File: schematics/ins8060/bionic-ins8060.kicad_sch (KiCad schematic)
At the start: 5 parts, among them J1 Bionic-P135, J2 Bionic-P245, U1 INS8060, U3 11AA010-I/TO

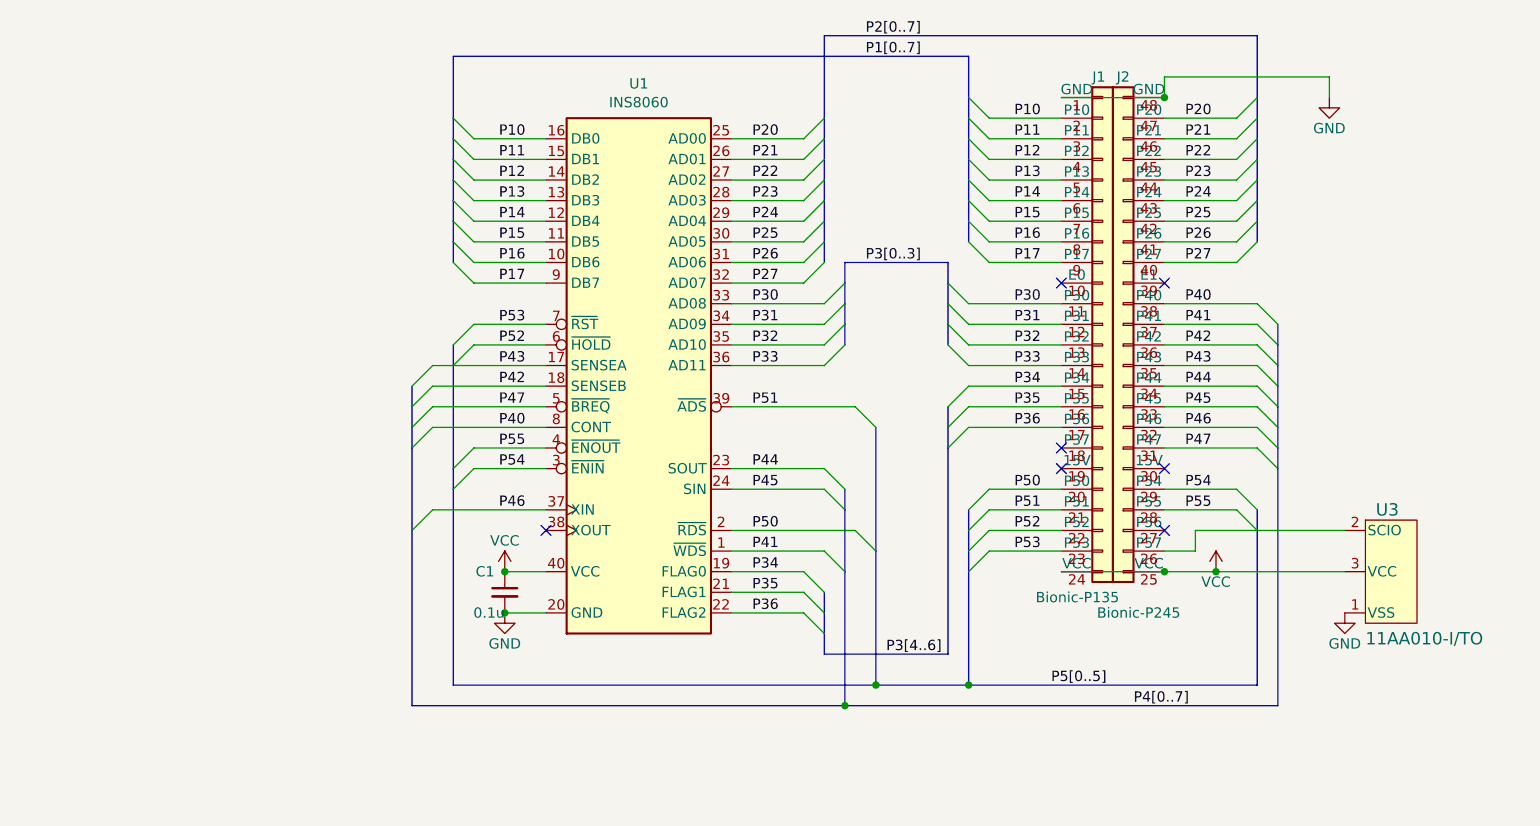
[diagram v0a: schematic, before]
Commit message: [INS8060] Add power LED
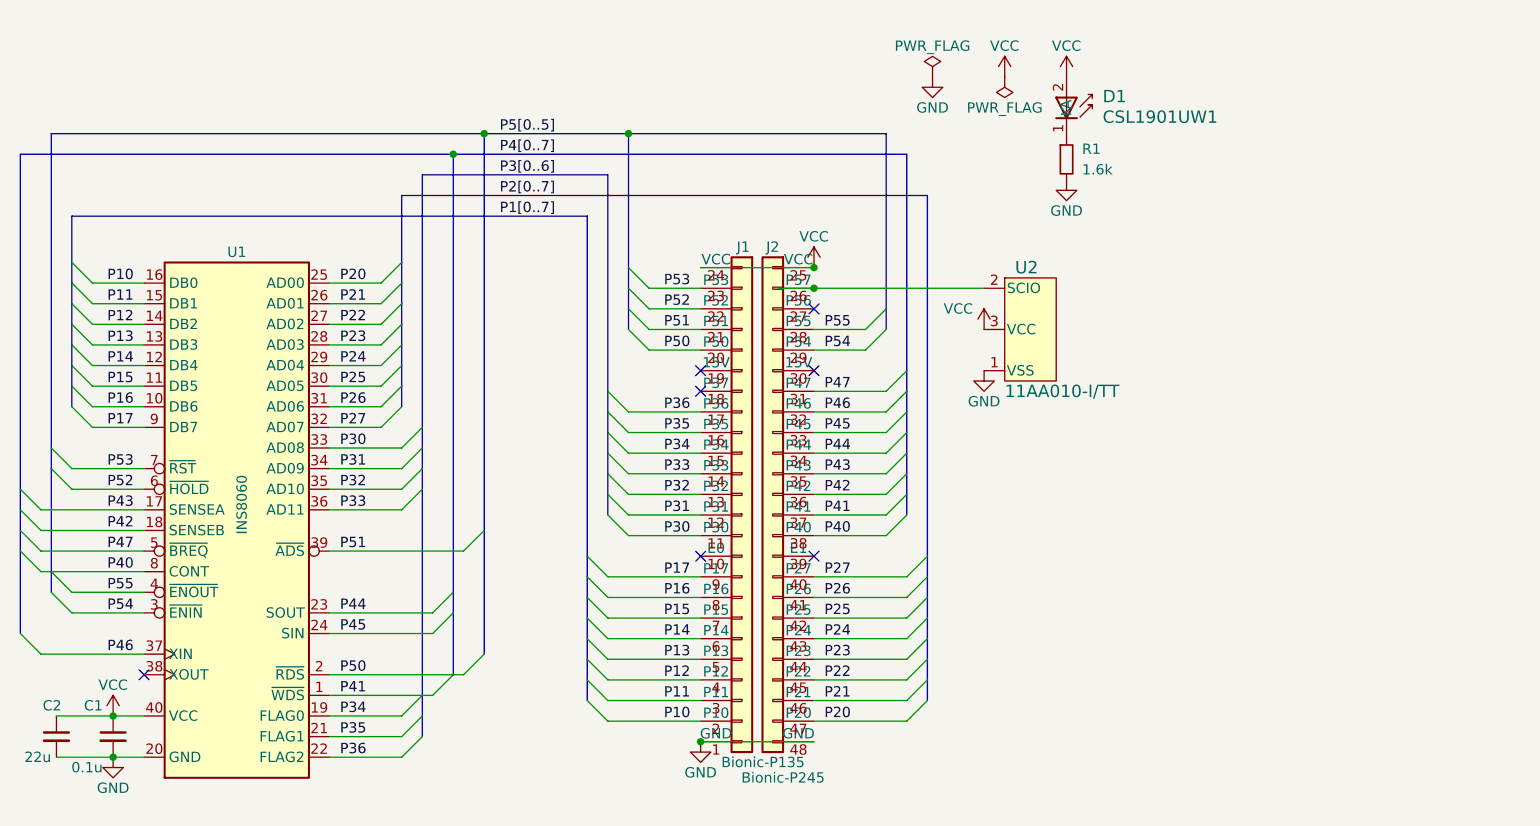
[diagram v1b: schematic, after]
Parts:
- removed U3: 11AA010-I/TO, TO-92_MC_MCH, symbol 0-LocalLibrary:11AA010-I_TO
- added C2: 22u, Capacitor_SMD:C_0603_1608Metric_Pad1.08x0.95mm_HandSolder, symbol Device:C_Small
- added D1: CSL1901UW1, 0-LocalLibrary:LED_CSL1901UW1_ROM, symbol 0-LocalLibrary:CSL1901UW1
- added R1: 1.6k, Resistor_SMD:R_0603_1608Metric_Pad0.98x0.95mm_HandSolder, symbol Device:R_Small
- added U2: 11AA010-I/TT, 0-LocalLibrary:SOT-23_MC_MCH-M, symbol 0-LocalLibrary:11AA010-I_TT
- C1: footprint Capacitor_THT:C_Disc_D3.4mm_W2.1mm_P2.50mm -> Capacitor_SMD:C_0603_1608Metric_Pad1.08x0.95mm_HandSolder
- J1: footprint connector:Bionic-P135_Vertical -> 0-LocalLibrary:Bionic-P135_Vertical
- J2: footprint connector:Bionic-P245_Vertical -> 0-LocalLibrary:Bionic-P245_Vertical
- U1: footprint Package_DIP:DIP-40_W15.24mm -> 0-LocalLibrary:DIP-40_W15.24mm_Socket
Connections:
- net GND: now also C2.2, R1.2, U2.1 (VSS)
- net VCC: now also C2.1, D1.2 (A), U2.3 (VCC)
- net at J2.26 (P57): now also U2.2 (SCIO)
- new net: D1.1 (K), R1.1
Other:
- moved on the sheet: C1, U1

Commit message: [INS8060] Fix EEPROM pinout
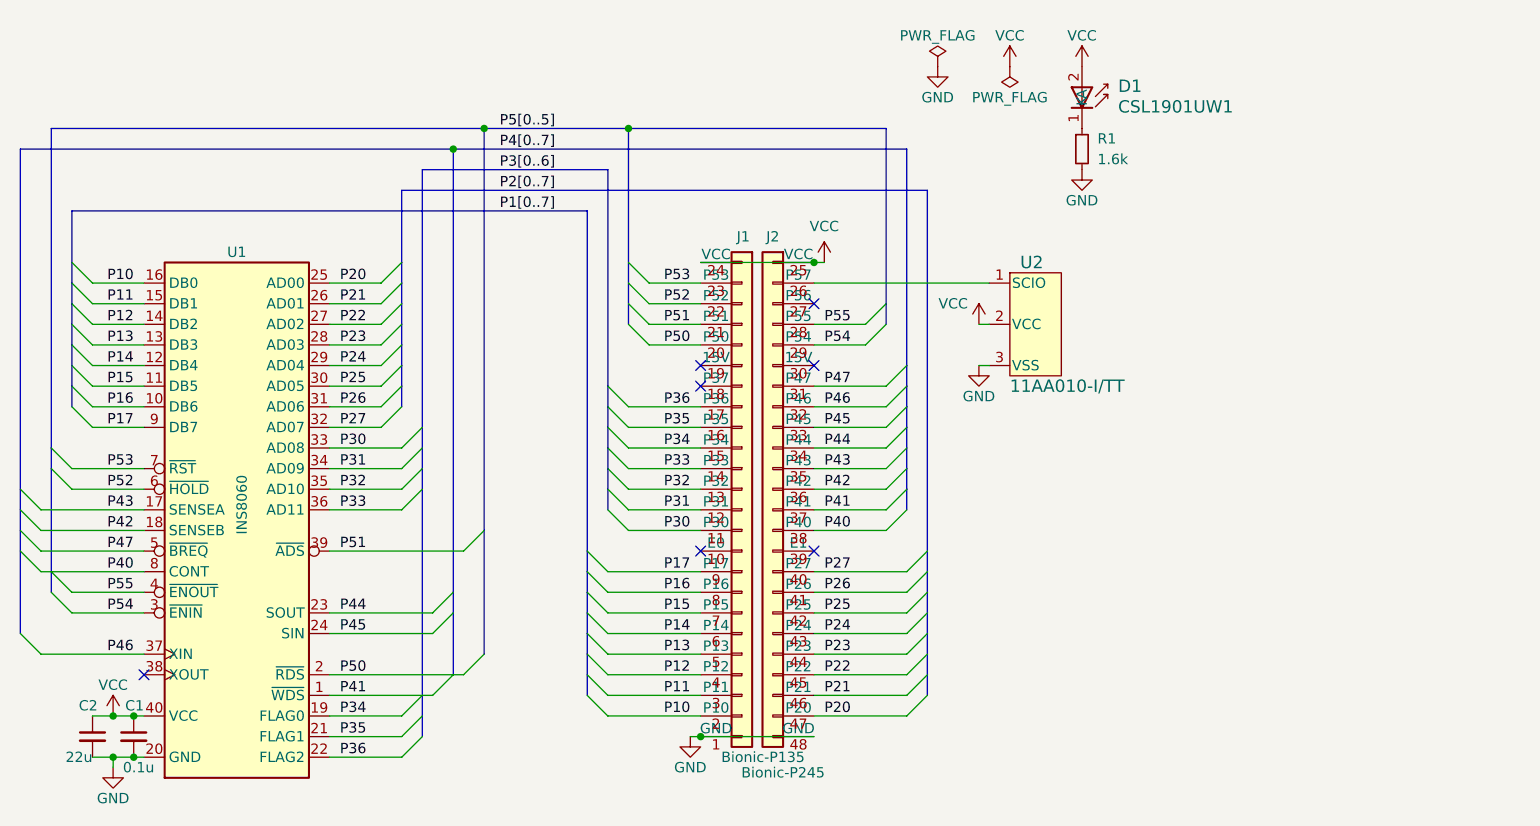
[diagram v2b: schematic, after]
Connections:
- net GND: now also U2.3 (VSS); no longer U2.1 (VSS)
- net VCC: now also U2.2 (VCC); no longer U2.3 (VCC)
- net at J2.26 (P57): now also U2.1 (SCIO); no longer U2.2 (SCIO)
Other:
- moved on the sheet: C1, C2, D1, J1, J2, R1, U2

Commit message: [schematics] Update LED footprint
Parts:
- D1: footprint 0-LocalLibrary:LED_CSL1901UW1_ROM -> 0-LocalLibrary:LED_CSL1901UW1_ROM-M

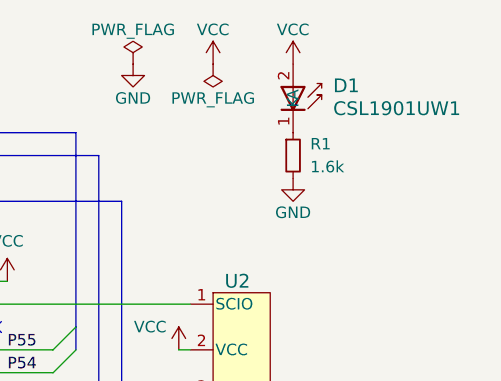
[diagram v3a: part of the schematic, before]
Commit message: [INS8060] Cleanup schematics
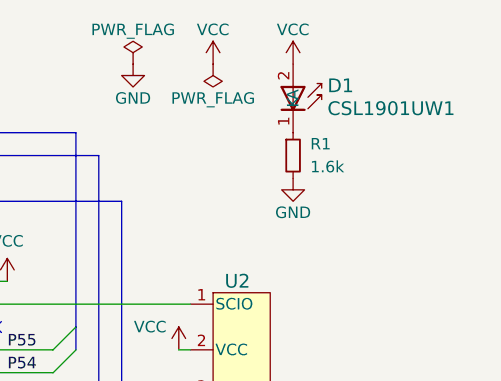
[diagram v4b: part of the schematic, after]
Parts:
- D1: footprint 0-LocalLibrary:LED_CSL1901UW1_ROM-M -> rhom:LED_CSL1901UW1_ROM-M; symbol 0-LocalLibrary:CSL1901UW1 -> rhom:CSL1901UW1
- J1: footprint 0-LocalLibrary:Bionic-P135_Vertical -> bionic:Bionic-P135_Vertical; symbol 0-LocalLibrary:Bionic-P135 -> bionic:Bionic-P135
- J2: footprint 0-LocalLibrary:Bionic-P245_Vertical -> bionic:Bionic-P245_Vertical; symbol 0-LocalLibrary:Bionic-P245 -> bionic:Bionic-P245
- U1: footprint 0-LocalLibrary:DIP-40_W15.24mm_Socket -> bionic:DIP-40_W15.24mm_Socket; symbol 0-LocalLibrary:INS8060 -> cpu:INS8060
- U2: footprint 0-LocalLibrary:SOT-23_MC_MCH-M -> microchip:SOT-23_MC_MCH-M; symbol 0-LocalLibrary:11AA010-I_TT -> microchip:11AA010-I_TT
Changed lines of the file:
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@@
 	)
 	(symbol
-		(lib_id "0-LocalLibrary:INS8060")
+		(lib_id "cpu:INS8060")
 		(at 86.36 97.79 0)
 		(unit 1)
@@
 			)
 		)
-		(property "Footprint" "0-LocalLibrary:DIP-40_W15.24mm_Socket"
+		(property "Footprint" "bionic:DIP-40_W15.24mm_Socket"
 			(at 87.63 132.08 0)
 			(effects
@@
 			)
 		)
-		(property "Description" ""
+		(property "Description" "8-bit General Purpose Microprocessor, DIP-40"
 			(at 86.36 97.79 0)
 			(effects
@@
 	)
 	(symbol
-		(lib_id "0-LocalLibrary:Bionic-P245")
+		(lib_id "bionic:Bionic-P245")
 		(at 156.21 95.25 0)
 		(unit 1)
@@
 			)
 		)
-		(property "Footprint" "0-LocalLibrary:Bionic-P245_Vertical"
+		(property "Footprint" "bionic:Bionic-P245_Vertical"
 			(at 157.48 130.81 0)
 			(effects
@@
 			)
 		)
-		(property "Description" ""
+		(property "Description" "Generic connector, single row, 01x24, script generated (kicad-library-utils/schlib/autogen/connector/)"
 			(at 156.21 95.25 0)
 			(effects
@@
 	)
 	(symbol
-		(lib_id "0-LocalLibrary:Bionic-P135")
+		(lib_id "bionic:Bionic-P135")
 		(at 148.59 95.25 0)
 		(unit 1)
@@
 			)
 		)
-		(property "Footprint" "0-LocalLibrary:Bionic-P135_Vertical"
+		(property "Footprint" "bionic:Bionic-P135_Vertical"
 			(at 149.86 130.81 0)
 			(effects
@@
 			)
 		)
-		(property "Description" ""
+		(property "Description" "Generic connector, single row, 01x24, script generated (kicad-library-utils/schlib/autogen/connector/)"
 			(at 148.59 95.25 0)
 			(effects
@@
 	)
 	(symbol
-		(lib_id "0-LocalLibrary:CSL1901UW1")
+		(lib_id "rhom:CSL1901UW1")
 		(at 190.5 43.18 270)
 		(unit 1)
@@
 		(fields_autoplaced yes)
 		(property "Reference" "D1"
-			(at 194.945 45.593 90)
+			(at 194.31 45.5929 90)
 			(effects
 				(font
@@
 		)
 		(property "Value" "CSL1901UW1"
-			(at 194.945 48.133 90)
+			(at 194.31 48.1329 90)
 			(effects
 				(font
@@
 			)
 		)
-		(property "Footprint" "0-LocalLibrary:LED_CSL1901UW1_ROM-M"
+		(property "Footprint" "rhom:LED_CSL1901UW1_ROM-M"
 			(at 181.61 46.99 0)
 			(effects
@@
 			)
 		)
-		(property "Description" ""
+		(property "Description" "Red LED (Low Current Emission, SMD)"
 			(at 190.5 43.18 0)
 			(effects
@@
 	)
 	(symbol
-		(lib_id "0-LocalLibrary:11AA010-I_TT")
+		(lib_id "microchip:11AA010-I_TT")
 		(at 181.61 68.58 0)
 		(unit 1)
@@
 			)
 		)
-		(property "Footprint" "0-LocalLibrary:SOT-23_MC_MCH-M"
+		(property "Footprint" "microchip:SOT-23_MC_MCH-M"
 			(at 184.15 86.36 0)
 			(effects
@@
 			)
 		)
-		(property "Description" ""
+		(property "Description" "UNI/O Serial EEPROM (1Kbit)"
 			(at 181.61 68.58 0)
 			(effects

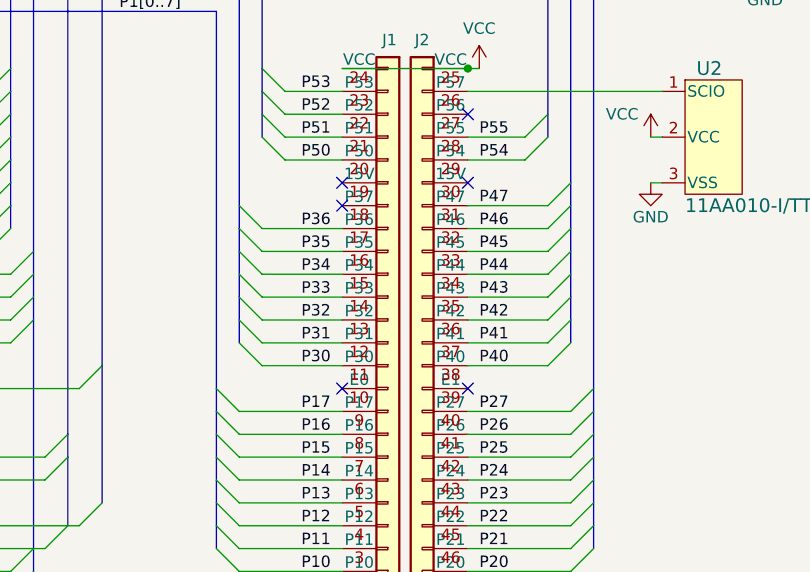
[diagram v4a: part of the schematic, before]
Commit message: [INS8060] Update schematics
Remove unused pins from bionic connector
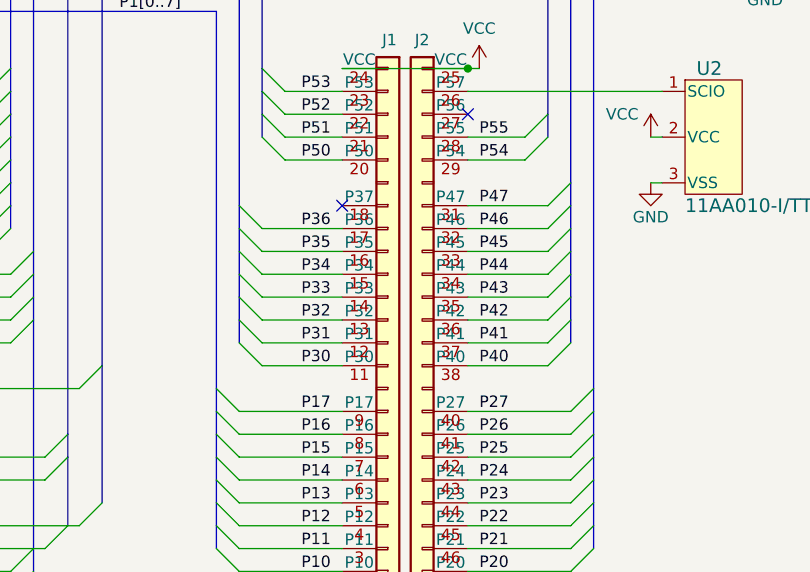
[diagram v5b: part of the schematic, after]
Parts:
- J1: footprint bionic:Bionic-P135_Vertical -> bionic:Bionic-P135_THT
- J2: footprint bionic:Bionic-P245_Vertical -> bionic:Bionic-P245_THT
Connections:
- no-connect marks 7 -> 3
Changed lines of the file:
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@@
 	(title_block
 		(title "BionicINS8060")
-		(date "2024-11-01")
-		(rev "6")
+		(date "2025-03-02")
+		(rev "7")
 		(company "Tadashi G. Takaoka")
 	)
@@
 	)
 	(no_connect
-		(at 157.48 80.01)
-	)
-	(no_connect
 		(at 74.93 118.11)
 	)
@@
 	)
 	(no_connect
-		(at 143.51 80.01)
-	)
-	(no_connect
 		(at 157.48 72.39)
 	)
-	(no_connect
-		(at 143.51 102.87)
-	)
-	(no_connect
-		(at 157.48 102.87)
-	)
 	(bus_entry
 		(at 134.62 72.39)
@@
 			)
 		)
-		(property "Footprint" "bionic:Bionic-P245_Vertical"
+		(property "Footprint" "bionic:Bionic-P245_THT"
 			(at 157.48 130.81 0)
 			(effects
@@
 		(pin "48"
 		)
-		(pin "39"
-		)
 		(pin "42"
 		)
@@
 		(pin "37"
 		)
-		(pin "30"
-		)
 		(pin "46"
 		)
@@
 			)
 		)
-		(property "Footprint" "bionic:Bionic-P135_Vertical"
+		(property "Footprint" "bionic:Bionic-P135_THT"
 			(at 149.86 130.81 0)
 			(effects
@@
 		(pin "21"
 		)
-		(pin "19"
-		)
 		(pin "7"
 		)
@@
 		(pin "11"
 		)
-		(pin "10"
-		)
 		(pin "1"
